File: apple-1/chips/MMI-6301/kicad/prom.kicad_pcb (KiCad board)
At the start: 4 copper layers, 19.6 x 9.4 mm, 25 parts, among them J1 DIP16_pins, U1 TLV743P 3.3V, U10 ICE40LP1K-CM36, U11 AT25DF041B, U2 TLV743P 1.2V, U3 74LVC2G34, U4 74LVC2G34, U5 74LVC2G34, U6 74LVC2G34, U7 74LVC2G34, U8 74LVC2G125, U9 74LVC2G125

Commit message: MMI-6301 preliminary layout
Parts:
- removed the TP4 at (148.6, 85.7)
- C1, C2, C3, R1, R2, U1, U2: moved to B.Cu
- moved TP3 6.22 mm to (156.2, 89.4)
- moved TP6 5.15 mm to (155.1, 89.4)
- moved TP4 4.05 mm to (155.3, 87.0)
- moved TP7 3.40 mm to (155.9, 87.5)
- moved R2 2.96 mm to (156.3, 88.3)
- moved TP5 2.63 mm to (151.1, 91.5)
- moved U11 1.87 mm to (153.1, 87.9), turned to 90 degrees
- moved C3 1.68 mm to (144.0, 87.9)
- moved U2 1.60 mm to (143.8, 86.5), turned to 90 degrees
- moved TP1 1.07 mm to (140.2, 90.0)
- moved U6 1.03 mm to (141.7, 87.2)
- moved U5 1.02 mm to (143.0, 90.3)
- moved TP2 0.56 mm to (144.4, 88.2)
- moved C2 0.49 mm to (140.3, 88.7)
- moved U10 0.33 mm to (148.6, 87.6)
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- renumbered TP5 to TP4, TP6 to TP5, TP7 to TP6, TP8 to TP7
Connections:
- U10 pad E1: A0 -> A3
- U10 pad E2: A3 -> A0
- U2 pad 3: +5V -> +3V3
- U2 pad 4: +5V -> +3V3
- U7 pad 1: /Sheet5E85C2D6/DIP_CE2_N -> /Sheet5E85C2D6/DIP_CE1_N
- U7 pad 3: /Sheet5E85C2D6/DIP_CE1_N -> /Sheet5E85C2D6/DIP_CE2_N
- U7 pad 4: CE1_N -> CE2_N
- U7 pad 6: CE2_N -> CE1_N
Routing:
- net GND: track 0.00 -> 14.5 mm, vias 0 -> 18
- net +3V3: track 0.00 -> 14.2 mm, vias 0 -> 17
- net OE_N: track 0.00 -> 13.8 mm, vias 0 -> 2
- net Net-(TP3-Pad1): track 0.00 -> 12.0 mm, vias 0 -> 2
- net Net-(TP4-Pad1): track 0.00 -> 10.3 mm, vias 0 -> 2
- net D3: track 0.00 -> 10.2 mm, vias 0 -> 2
- net Net-(TP6-Pad1): track 0.00 -> 9.71 mm, vias 0 -> 2
- net Net-(R2-Pad2): track 0.00 -> 9.41 mm, vias 0 -> 2
- net D2: track 0.00 -> 7.74 mm, vias 0 -> 2
- net A2: track 0.00 -> 6.94 mm, vias 0 -> 2
- net A1: track 0.00 -> 6.57 mm, vias 0 -> 2
- net A5: track 0.00 -> 6.36 mm
- net +1V2: track 0.00 -> 6.26 mm, vias 0 -> 1
- net D1: track 0.00 -> 6.24 mm
- net A6: track 0.00 -> 5.88 mm
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- added copper zone on In2.Cu, net +3V3
- added copper zone on In1.Cu, net GND
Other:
- net class Default: clearance 0.1524 -> 0.099822; trace_width 0.1524 -> 0.099822; via_dia 0.508 -> 0.4064; via_drill 0.3048 -> 0.2032
- rule pad_to_mask_clearance: 0.0635 -> 0.04826
- rule solder_mask_min_width: 0.1016 -> 0.04064
- rule trace_clearance: 0.1524 -> 0.099822
- rule trace_min: 0.1524 -> 0.099822
- rule via_min_drill: 0.3048 -> 0.2032
- rule via_min_size: 0.508 -> 0.4064

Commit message: completed layout
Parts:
- TP1, TP2, TP3, TP4, TP5, TP6, TP7: footprint prom:test-point-25 -> prom:test-point
- moved TP7 1.42 mm to (157.4, 87.4)
- moved TP6 1.22 mm to (155.9, 90.2)
- moved TP2 1.15 mm to (145.2, 87.5), turned to 180 degrees
- moved TP4 0.97 mm to (156.2, 87.3)
- moved TP3 0.96 mm to (157.1, 89.8)
- moved TP1 0.81 mm to (140.8, 89.4)
- moved TP5 0.47 mm to (151.1, 91.1)
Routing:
- net Net-(R2-Pad2): track 9.41 -> 12.4 mm
- net Net-(TP6-Pad1): track 9.71 -> 11.4 mm, vias 2 -> 1
- net Net-(TP3-Pad1): track 12.0 -> 13.5 mm
- net +1V2: track 6.26 -> 4.85 mm, vias 1 -> 0
- net Net-(TP4-Pad1): track 10.3 -> 11.2 mm
- net A2: track 6.94 -> 6.19 mm
- net /Sheet5E85C2D6/DIP_D3: track 4.89 -> 5.46 mm
- net Net-(R1-Pad2): track 4.63 -> 4.15 mm, vias 2 -> 1
- net +3V3: track 14.2 -> 14.0 mm, vias 17 -> 16
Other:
- net class Default: via_dia 0.4064 -> 0.508; via_drill 0.2032 -> 0.254
- rule via_min_drill: 0.2032 -> 0.254
- rule via_min_size: 0.4064 -> 0.508

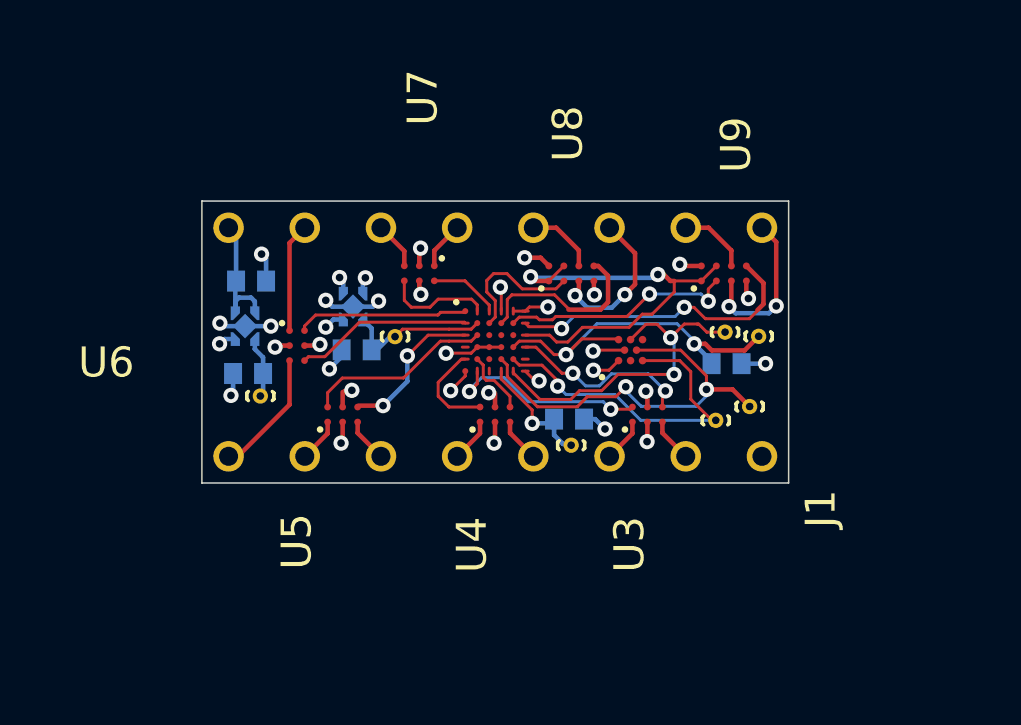
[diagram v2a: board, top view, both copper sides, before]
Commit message: minor layout updates:  make vias partially tented (by postprocessing gerber files); redefine NSMD pads on the X2SON footprint; add silkscreen text
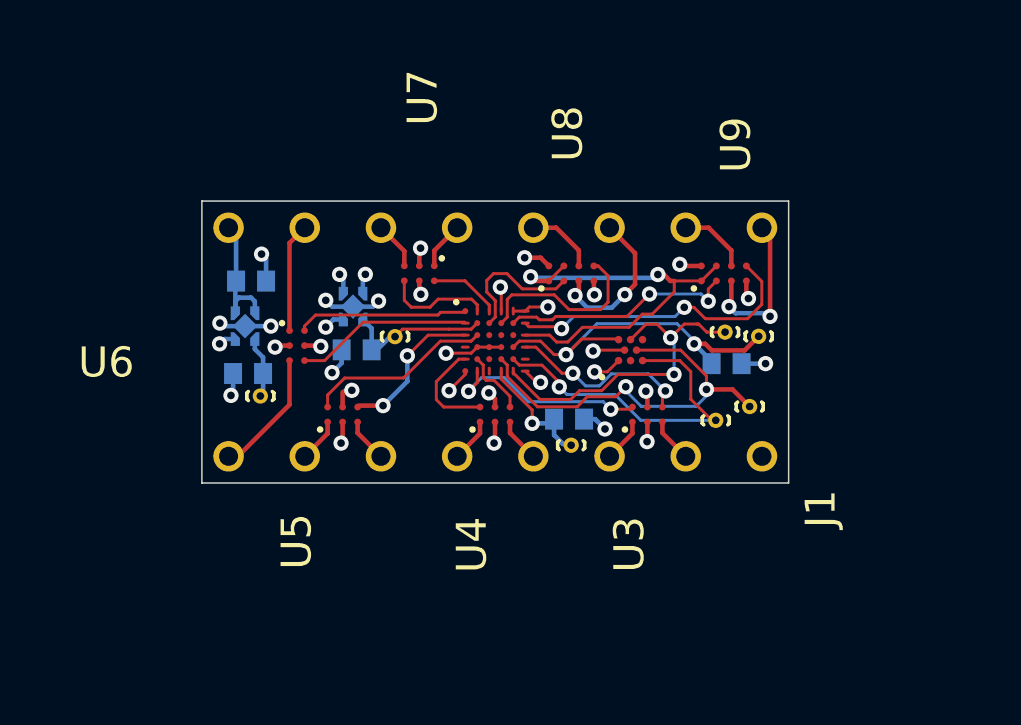
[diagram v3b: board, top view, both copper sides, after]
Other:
- board text added: "MMI 6301 version 0.5 April 2020 Peter Monta"
